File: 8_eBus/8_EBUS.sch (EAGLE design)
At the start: 19 parts, among them IC1 MCP6542, Q1 BC817, X1 AKL18X-02W, X2 ALLSERIALSLAVE

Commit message: Cleanup, front with lib elements
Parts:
- R5: value 270 -> 180
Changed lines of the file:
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@@
 <?xml version="1.0" encoding="utf-8"?>
 <!DOCTYPE eagle SYSTEM "eagle.dtd">
-<eagle version="7.6.0">
+<eagle version="7.7.0">
 <drawing>
 <settings>
@@
 <grid distance="0.1" unitdist="inch" unit="inch" style="lines" multiple="1" display="no" altdistance="0.01" altunitdist="inch" altunit="inch"/>
 <layers>
-<layer number="1" name="Top" color="4" fill="1" visible="no" active="no"/>
-<layer number="2" name="Route2" color="1" fill="3" visible="no" active="no"/>
-<layer number="3" name="Route3" color="4" fill="3" visible="no" active="no"/>
-<layer number="4" name="Route4" color="1" fill="4" visible="no" active="no"/>
-<layer number="5" name="Route5" color="4" fill="4" visible="no" active="no"/>
-<layer number="6" name="Route6" color="1" fill="8" visible="no" active="no"/>
-<layer number="7" name="Route7" color="4" fill="8" visible="no" active="no"/>
-<layer number="8" name="Route8" color="1" fill="2" visible="no" active="no"/>
-<layer number="9" name="Route9" color="4" fill="2" visible="no" active="no"/>
-<layer number="10" name="Route10" color="1" fill="7" visible="no" active="no"/>
-<layer number="11" name="Route11" color="4" fill="7" visible="no" active="no"/>
-<layer number="12" name="Route12" color="1" fill="5" visible="no" active="no"/>
-<layer number="13" name="Route13" color="4" fill="5" visible="no" active="no"/>
-<layer number="14" name="Route14" color="1" fill="6" visible="no" active="no"/>
-<layer number="15" name="Route15" color="4" fill="6" visible="no" active="no"/>
-<layer number="16" name="Bottom" color="1" fill="1" visible="no" active="no"/>
-<layer number="17" name="Pads" color="2" fill="1" visible="no" active="no"/>
-<layer number="18" name="Vias" color="2" fill="1" visible="no" active="no"/>
-<layer number="19" name="Unrouted" color="6" fill="1" visible="no" active="no"/>
-<layer number="20" name="Dimension" color="15" fill="1" visible="no" active="no"/>
-<layer number="21" name="tPlace" color="7" fill="1" visible="no" active="no"/>
-<layer number="22" name="bPlace" color="7" fill="1" visible="no" active="no"/>
-<layer number="23" name="tOrigins" color="15" fill="1" visible="no" active="no"/>
-<layer number="24" name="bOrigins" color="15" fill="1" visible="no" active="no"/>
-<layer number="25" name="tNames" color="7" fill="1" visible="no" active="no"/>
-<layer number="26" name="bNames" color="7" fill="1" visible="no" active="no"/>
-<layer number="27" name="tValues" color="7" fill="1" visible="no" active="no"/>
-<layer number="28" name="bValues" color="7" fill="1" visible="no" active="no"/>
+<layer number="1" name="Top" color="4" fill="1" visible="yes" active="no"/>
+<layer number="2" name="Route2" color="1" fill="3" visible="yes" active="no"/>
+<layer number="3" name="Route3" color="4" fill="3" visible="yes" active="no"/>
+<layer number="4" name="Route4" color="1" fill="4" visible="yes" active="no"/>
+<layer number="5" name="Route5" color="4" fill="4" visible="yes" active="no"/>
+<layer number="6" name="Route6" color="1" fill="8" visible="yes" active="no"/>
+<layer number="7" name="Route7" color="4" fill="8" visible="yes" active="no"/>
+<layer number="8" name="Route8" color="1" fill="2" visible="yes" active="no"/>
+<layer number="9" name="Route9" color="4" fill="2" visible="yes" active="no"/>
+<layer number="10" name="Route10" color="1" fill="7" visible="yes" active="no"/>
+<layer number="11" name="Route11" color="4" fill="7" visible="yes" active="no"/>
+<layer number="12" name="Route12" color="1" fill="5" visible="yes" active="no"/>
+<layer number="13" name="Route13" color="4" fill="5" visible="yes" active="no"/>
+<layer number="14" name="Route14" color="1" fill="6" visible="yes" active="no"/>
+<layer number="15" name="Route15" color="4" fill="6" visible="yes" active="no"/>
+<layer number="16" name="Bottom" color="1" fill="1" visible="yes" active="no"/>
+<layer number="17" name="Pads" color="2" fill="1" visible="yes" active="no"/>
+<layer number="18" name="Vias" color="2" fill="1" visible="yes" active="no"/>
+<layer number="19" name="Unrouted" color="6" fill="1" visible="yes" active="no"/>
+<layer number="20" name="Dimension" color="15" fill="1" visible="yes" active="no"/>
+<layer number="21" name="tPlace" color="7" fill="1" visible="yes" active="no"/>
+<layer number="22" name="bPlace" color="7" fill="1" visible="yes" active="no"/>
+<layer number="23" name="tOrigins" color="15" fill="1" visible="yes" active="no"/>
+<layer number="24" name="bOrigins" color="15" fill="1" visible="yes" active="no"/>
+<layer number="25" name="tNames" color="7" fill="1" visible="yes" active="no"/>
+<layer number="26" name="bNames" color="7" fill="1" visible="yes" active="no"/>
+<layer number="27" name="tValues" color="7" fill="1" visible="yes" active="no"/>
+<layer number="28" name="bValues" color="7" fill="1" visible="yes" active="no"/>
 <layer number="29" name="tStop" color="7" fill="3" visible="no" active="no"/>
 <layer number="30" name="bStop" color="7" fill="6" visible="no" active="no"/>
@@
 <layer number="35" name="tGlue" color="7" fill="4" visible="no" active="no"/>
 <layer number="36" name="bGlue" color="7" fill="5" visible="no" active="no"/>
-<layer number="37" name="tTest" color="7" fill="1" visible="no" active="no"/>
-<layer number="38" name="bTest" color="7" fill="1" visible="no" active="no"/>
+<layer number="37" name="tTest" color="7" fill="1" visible="yes" active="no"/>
+<layer number="38" name="bTest" color="7" fill="1" visible="yes" active="no"/>
 <layer number="39" name="tKeepout" color="4" fill="11" visible="no" active="no"/>
 <layer number="40" name="bKeepout" color="1" fill="11" visible="no" active="no"/>
@@
 <layer number="44" name="Drills" color="7" fill="1" visible="no" active="no"/>
 <layer number="45" name="Holes" color="7" fill="1" visible="no" active="no"/>
-<layer number="46" name="Milling" color="3" fill="1" visible="no" active="no"/>
-<layer number="47" name="Measures" color="7" fill="1" visible="no" active="no"/>
-<layer number="48" name="Document" color="7" fill="1" visible="no" active="no"/>
-<layer number="49" name="Reference" color="7" fill="1" visible="no" active="no"/>
-<layer number="50" name="dxf" color="7" fill="1" visible="no" active="no"/>
-<layer number="51" name="tDocu" color="7" fill="1" visible="no" active="no"/>
-<layer number="52" name="bDocu" color="7" fill="1" visible="no" active="no"/>
-<layer number="53" name="tGND_GNDA" color="7" fill="9" visible="no" active="no"/>
-<layer number="54" name="bGND_GNDA" color="1" fill="9" visible="no" active="no"/>
-<layer number="56" name="wert" color="7" fill="1" visible="no" active="no"/>
-<layer number="57" name="tCAD" color="7" fill="1" visible="no" active="no"/>
-<layer number="58" name="bCAD" color="11" fill="1" visible="no" active="no"/>
-<layer number="59" name="tCarbon" color="7" fill="1" visible="no" active="no"/>
-<layer number="60" name="bCarbon" color="7" fill="1" visible="no" active="no"/>
-<layer number="61" name="pt_docu" color="7" fill="0" visible="no" active="no"/>
+<layer number="46" name="Milling" color="3" fill="1" visible="yes" active="no"/>
+<layer number="47" name="Measures" color="7" fill="1" visible="yes" active="no"/>
+<layer number="48" name="Document" color="7" fill="1" visible="yes" active="no"/>
+<layer number="49" name="Reference" color="7" fill="1" visible="yes" active="no"/>
+<layer number="50" name="dxf" color="7" fill="1" visible="yes" active="no"/>
+<layer number="51" name="tDocu" color="7" fill="1" visible="yes" active="no"/>
+<layer number="52" name="bDocu" color="7" fill="1" visible="yes" active="no"/>
+<layer number="53" name="tGND_GNDA" color="7" fill="9" visible="yes" active="no"/>
+<layer number="54" name="bGND_GNDA" color="1" fill="9" visible="yes" active="no"/>
+<layer number="56" name="wert" color="7" fill="1" visible="yes" active="no"/>
+<layer number="57" name="tCAD" color="7" fill="1" visible="yes" active="no"/>
+<layer number="58" name="bCAD" color="11" fill="1" visible="yes" active="no"/>
+<layer number="59" name="tCarbon" color="7" fill="1" visible="yes" active="no"/>
+<layer number="60" name="bCarbon" color="7" fill="1" visible="yes" active="no"/>
+<layer number="61" name="pt_docu" color="7" fill="0" visible="yes" active="no"/>
 <layer number="90" name="Modules" color="5" fill="1" visible="yes" active="yes"/>
 <layer number="91" name="Nets" color="2" fill="1" visible="yes" active="yes"/>
@@
 <part name="LED1" library="led" deviceset="LED" device="CHIPLED_0805"/>
 <part name="GND8" library="supply1" deviceset="GND" device=""/>
-<part name="R5" library="rcl" deviceset="R-EU_" device="R0805" value="270"/>
+<part name="R5" library="rcl" deviceset="R-EU_" device="R0805" value="180"/>
 <part name="GND9" library="supply1" deviceset="GND" device=""/>
 <part name="P+6" library="supply1" deviceset="VCC/2" device=""/>

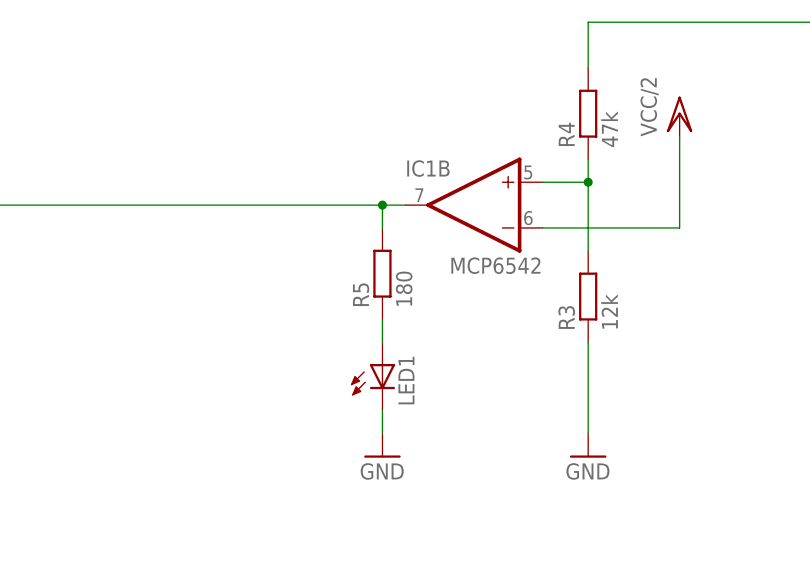
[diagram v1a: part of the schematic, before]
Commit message: pro mini layout corrected
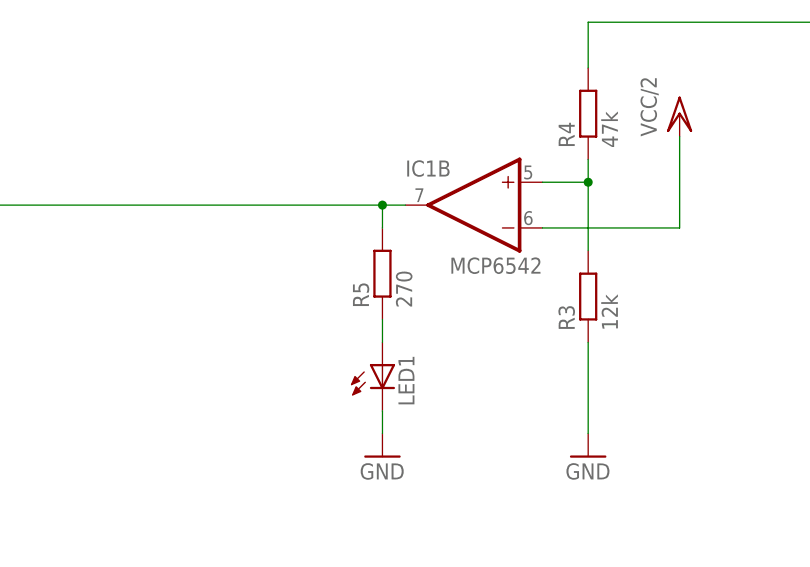
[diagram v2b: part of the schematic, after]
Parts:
- R5: value 180 -> 270
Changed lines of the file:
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@@
 <?xml version="1.0" encoding="utf-8"?>
 <!DOCTYPE eagle SYSTEM "eagle.dtd">
-<eagle version="7.7.0">
+<eagle version="7.6.0">
 <drawing>
 <settings>
@@
 <grid distance="0.1" unitdist="inch" unit="inch" style="lines" multiple="1" display="no" altdistance="0.01" altunitdist="inch" altunit="inch"/>
 <layers>
-<layer number="1" name="Top" color="4" fill="1" visible="yes" active="no"/>
-<layer number="2" name="Route2" color="1" fill="3" visible="yes" active="no"/>
-<layer number="3" name="Route3" color="4" fill="3" visible="yes" active="no"/>
-<layer number="4" name="Route4" color="1" fill="4" visible="yes" active="no"/>
-<layer number="5" name="Route5" color="4" fill="4" visible="yes" active="no"/>
-<layer number="6" name="Route6" color="1" fill="8" visible="yes" active="no"/>
-<layer number="7" name="Route7" color="4" fill="8" visible="yes" active="no"/>
-<layer number="8" name="Route8" color="1" fill="2" visible="yes" active="no"/>
-<layer number="9" name="Route9" color="4" fill="2" visible="yes" active="no"/>
-<layer number="10" name="Route10" color="1" fill="7" visible="yes" active="no"/>
-<layer number="11" name="Route11" color="4" fill="7" visible="yes" active="no"/>
-<layer number="12" name="Route12" color="1" fill="5" visible="yes" active="no"/>
-<layer number="13" name="Route13" color="4" fill="5" visible="yes" active="no"/>
-<layer number="14" name="Route14" color="1" fill="6" visible="yes" active="no"/>
-<layer number="15" name="Route15" color="4" fill="6" visible="yes" active="no"/>
-<layer number="16" name="Bottom" color="1" fill="1" visible="yes" active="no"/>
-<layer number="17" name="Pads" color="2" fill="1" visible="yes" active="no"/>
-<layer number="18" name="Vias" color="2" fill="1" visible="yes" active="no"/>
-<layer number="19" name="Unrouted" color="6" fill="1" visible="yes" active="no"/>
-<layer number="20" name="Dimension" color="15" fill="1" visible="yes" active="no"/>
-<layer number="21" name="tPlace" color="7" fill="1" visible="yes" active="no"/>
-<layer number="22" name="bPlace" color="7" fill="1" visible="yes" active="no"/>
-<layer number="23" name="tOrigins" color="15" fill="1" visible="yes" active="no"/>
-<layer number="24" name="bOrigins" color="15" fill="1" visible="yes" active="no"/>
-<layer number="25" name="tNames" color="7" fill="1" visible="yes" active="no"/>
-<layer number="26" name="bNames" color="7" fill="1" visible="yes" active="no"/>
-<layer number="27" name="tValues" color="7" fill="1" visible="yes" active="no"/>
-<layer number="28" name="bValues" color="7" fill="1" visible="yes" active="no"/>
+<layer number="1" name="Top" color="4" fill="1" visible="no" active="no"/>
+<layer number="2" name="Route2" color="1" fill="3" visible="no" active="no"/>
+<layer number="3" name="Route3" color="4" fill="3" visible="no" active="no"/>
+<layer number="4" name="Route4" color="1" fill="4" visible="no" active="no"/>
+<layer number="5" name="Route5" color="4" fill="4" visible="no" active="no"/>
+<layer number="6" name="Route6" color="1" fill="8" visible="no" active="no"/>
+<layer number="7" name="Route7" color="4" fill="8" visible="no" active="no"/>
+<layer number="8" name="Route8" color="1" fill="2" visible="no" active="no"/>
+<layer number="9" name="Route9" color="4" fill="2" visible="no" active="no"/>
+<layer number="10" name="Route10" color="1" fill="7" visible="no" active="no"/>
+<layer number="11" name="Route11" color="4" fill="7" visible="no" active="no"/>
+<layer number="12" name="Route12" color="1" fill="5" visible="no" active="no"/>
+<layer number="13" name="Route13" color="4" fill="5" visible="no" active="no"/>
+<layer number="14" name="Route14" color="1" fill="6" visible="no" active="no"/>
+<layer number="15" name="Route15" color="4" fill="6" visible="no" active="no"/>
+<layer number="16" name="Bottom" color="1" fill="1" visible="no" active="no"/>
+<layer number="17" name="Pads" color="2" fill="1" visible="no" active="no"/>
+<layer number="18" name="Vias" color="2" fill="1" visible="no" active="no"/>
+<layer number="19" name="Unrouted" color="6" fill="1" visible="no" active="no"/>
+<layer number="20" name="Dimension" color="15" fill="1" visible="no" active="no"/>
+<layer number="21" name="tPlace" color="7" fill="1" visible="no" active="no"/>
+<layer number="22" name="bPlace" color="7" fill="1" visible="no" active="no"/>
+<layer number="23" name="tOrigins" color="15" fill="1" visible="no" active="no"/>
+<layer number="24" name="bOrigins" color="15" fill="1" visible="no" active="no"/>
+<layer number="25" name="tNames" color="7" fill="1" visible="no" active="no"/>
+<layer number="26" name="bNames" color="7" fill="1" visible="no" active="no"/>
+<layer number="27" name="tValues" color="7" fill="1" visible="no" active="no"/>
+<layer number="28" name="bValues" color="7" fill="1" visible="no" active="no"/>
 <layer number="29" name="tStop" color="7" fill="3" visible="no" active="no"/>
 <layer number="30" name="bStop" color="7" fill="6" visible="no" active="no"/>
@@
 <layer number="35" name="tGlue" color="7" fill="4" visible="no" active="no"/>
 <layer number="36" name="bGlue" color="7" fill="5" visible="no" active="no"/>
-<layer number="37" name="tTest" color="7" fill="1" visible="yes" active="no"/>
-<layer number="38" name="bTest" color="7" fill="1" visible="yes" active="no"/>
+<layer number="37" name="tTest" color="7" fill="1" visible="no" active="no"/>
+<layer number="38" name="bTest" color="7" fill="1" visible="no" active="no"/>
 <layer number="39" name="tKeepout" color="4" fill="11" visible="no" active="no"/>
 <layer number="40" name="bKeepout" color="1" fill="11" visible="no" active="no"/>
@@
 <layer number="44" name="Drills" color="7" fill="1" visible="no" active="no"/>
 <layer number="45" name="Holes" color="7" fill="1" visible="no" active="no"/>
-<layer number="46" name="Milling" color="3" fill="1" visible="yes" active="no"/>
-<layer number="47" name="Measures" color="7" fill="1" visible="yes" active="no"/>
-<layer number="48" name="Document" color="7" fill="1" visible="yes" active="no"/>
-<layer number="49" name="Reference" color="7" fill="1" visible="yes" active="no"/>
-<layer number="50" name="dxf" color="7" fill="1" visible="yes" active="no"/>
-<layer number="51" name="tDocu" color="7" fill="1" visible="yes" active="no"/>
-<layer number="52" name="bDocu" color="7" fill="1" visible="yes" active="no"/>
-<layer number="53" name="tGND_GNDA" color="7" fill="9" visible="yes" active="no"/>
-<layer number="54" name="bGND_GNDA" color="1" fill="9" visible="yes" active="no"/>
-<layer number="56" name="wert" color="7" fill="1" visible="yes" active="no"/>
-<layer number="57" name="tCAD" color="7" fill="1" visible="yes" active="no"/>
-<layer number="58" name="bCAD" color="11" fill="1" visible="yes" active="no"/>
-<layer number="59" name="tCarbon" color="7" fill="1" visible="yes" active="no"/>
-<layer number="60" name="bCarbon" color="7" fill="1" visible="yes" active="no"/>
-<layer number="61" name="pt_docu" color="7" fill="0" visible="yes" active="no"/>
+<layer number="46" name="Milling" color="3" fill="1" visible="no" active="no"/>
+<layer number="47" name="Measures" color="7" fill="1" visible="no" active="no"/>
+<layer number="48" name="Document" color="7" fill="1" visible="no" active="no"/>
+<layer number="49" name="Reference" color="7" fill="1" visible="no" active="no"/>
+<layer number="50" name="dxf" color="7" fill="1" visible="no" active="no"/>
+<layer number="51" name="tDocu" color="7" fill="1" visible="no" active="no"/>
+<layer number="52" name="bDocu" color="7" fill="1" visible="no" active="no"/>
+<layer number="53" name="tGND_GNDA" color="7" fill="9" visible="no" active="no"/>
+<layer number="54" name="bGND_GNDA" color="1" fill="9" visible="no" active="no"/>
+<layer number="56" name="wert" color="7" fill="1" visible="no" active="no"/>
+<layer number="57" name="tCAD" color="7" fill="1" visible="no" active="no"/>
+<layer number="58" name="bCAD" color="11" fill="1" visible="no" active="no"/>
+<layer number="59" name="tCarbon" color="7" fill="1" visible="no" active="no"/>
+<layer number="60" name="bCarbon" color="7" fill="1" visible="no" active="no"/>
+<layer number="61" name="pt_docu" color="7" fill="0" visible="no" active="no"/>
 <layer number="90" name="Modules" color="5" fill="1" visible="yes" active="yes"/>
 <layer number="91" name="Nets" color="2" fill="1" visible="yes" active="yes"/>
@@
 <part name="LED1" library="led" deviceset="LED" device="CHIPLED_0805"/>
 <part name="GND8" library="supply1" deviceset="GND" device=""/>
-<part name="R5" library="rcl" deviceset="R-EU_" device="R0805" value="180"/>
+<part name="R5" library="rcl" deviceset="R-EU_" device="R0805" value="270"/>
 <part name="GND9" library="supply1" deviceset="GND" device=""/>
 <part name="P+6" library="supply1" deviceset="VCC/2" device=""/>
